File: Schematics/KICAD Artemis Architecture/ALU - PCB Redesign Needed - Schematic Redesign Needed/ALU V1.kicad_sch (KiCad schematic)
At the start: 11 parts, among them J1 B Input Socket, J2 A Input Socket, J3 F Output Socket, J4 Control Word Socket, J5 Flag Socket, J6 Power Socket, U1 74LS181, U2 74LS181, U3 74LS30

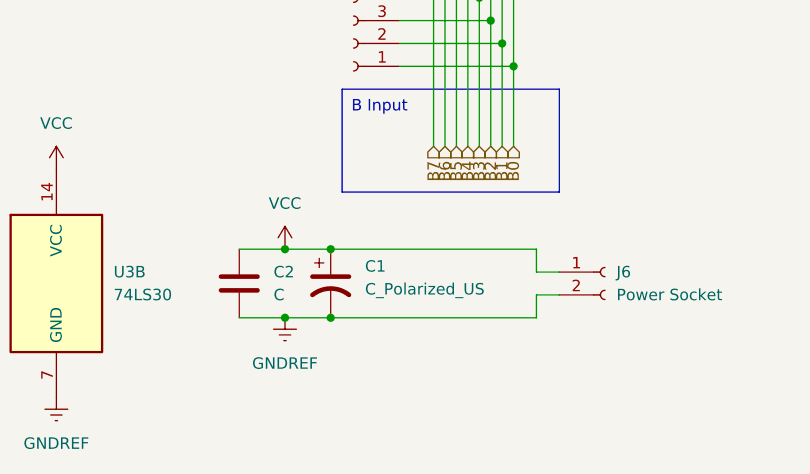
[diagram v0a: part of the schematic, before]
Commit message: Started ALU redesign
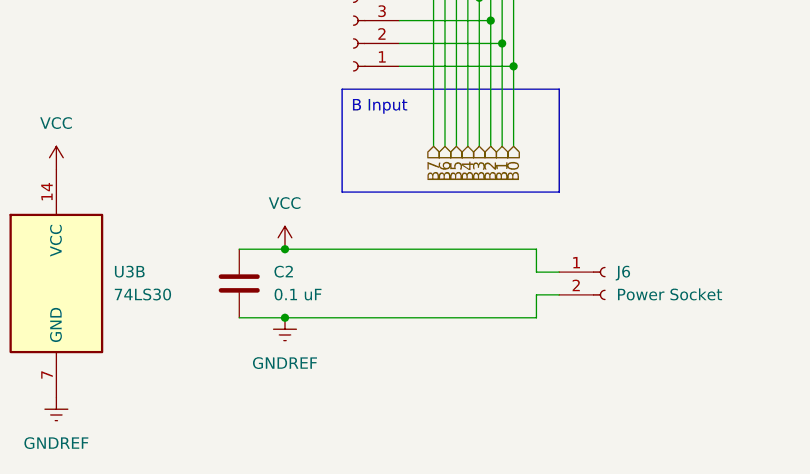
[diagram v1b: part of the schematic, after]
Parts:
- removed C1: C_Polarized_US, Capacitor_THT:CP_Radial_D10.0mm_P5.00mm, symbol Device:C_Polarized_US
- C2: value C -> 0.1 uF; footprint Capacitor_THT:C_Disc_D3.0mm_W2.0mm_P2.50mm -> Capacitor_SMD:C_1206_3216Metric_Pad1.33x1.80mm_HandSolder
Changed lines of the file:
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@@
 	)
 	(junction
-		(at 78.74 172.72)
-		(diameter 0)
-		(color 0 0 0 0)
-	)
-	(junction
 		(at 95.25 40.64)
 		(diameter 0)
@@
 	)
 	(junction
-		(at 78.74 180.34)
-		(diameter 0)
-		(color 0 0 0 0)
-	)
-	(junction
 		(at 93.98 142.24)
 		(diameter 0)
@@
 	(wire
 		(pts
-			(xy 101.6 180.34) (xy 78.74 180.34)
+			(xy 73.66 180.34) (xy 101.6 180.34)
 		)
 		(stroke
@@
 	(wire
 		(pts
-			(xy 73.66 172.72) (xy 78.74 172.72)
-		)
-		(stroke
-			(width 0)
-			(type default)
-		)
-	)
-	(wire
-		(pts
 			(xy 191.77 57.15) (xy 191.77 88.9)
 		)
@@
 	(wire
 		(pts
-			(xy 73.66 180.34) (xy 78.74 180.34)
-		)
-		(stroke
-			(width 0)
-			(type default)
-		)
-	)
-	(wire
-		(pts
 			(xy 86.36 149.86) (xy 97.79 149.86)
 		)
@@
 	(wire
 		(pts
-			(xy 101.6 172.72) (xy 78.74 172.72)
+			(xy 73.66 172.72) (xy 101.6 172.72)
 		)
 		(stroke
@@
 			)
 		)
-		(property "Value" "C"
+		(property "Value" "0.1 uF"
 			(at 72.39 177.7999 0)
 			(effects
@@
 			)
 		)
-		(property "Footprint" "Capacitor_THT:C_Disc_D3.0mm_W2.0mm_P2.50mm"
+		(property "Footprint" "Capacitor_SMD:C_1206_3216Metric_Pad1.33x1.80mm_HandSolder"
 			(at 69.5452 180.34 0)
 			(effects
@@
 					(unit 1)
 				)
-			)
-		)
-	)
-	(symbol
-		(lib_id "Device:C_Polarized_US")
-		(at 78.74 176.53 0)
-		(unit 1)
-		(exclude_from_sim no)
-		(in_bom yes)
-		(on_board yes)
-		(dnp no)
-		(fields_autoplaced yes)
-		(property "Reference" "C1"
-			(at 82.55 174.6249 0)
-			(effects
-				(font
-					(size 1.27 1.27)
-				)
-				(justify left)
-			)
-		)
-		(property "Value" "C_Polarized_US"
-			(at 82.55 177.1649 0)
-			(effects
-				(font
-					(size 1.27 1.27)
-				)
-				(justify left)
-			)
-		)
-		(property "Footprint" "Capacitor_THT:CP_Radial_D10.0mm_P5.00mm"
-			(at 78.74 176.53 0)
-			(effects
-				(font
-					(size 1.27 1.27)
-				)
-				(hide yes)
-			)
-		)
-		(property "Datasheet" "~"
-			(at 78.74 176.53 0)
-			(effects
-				(font
-					(size 1.27 1.27)
-				)
-				(hide yes)
-			)
-		)
-		(property "Description" "Polarized capacitor, US symbol"
-			(at 78.74 176.53 0)
-			(effects
-				(font
-					(size 1.27 1.27)
-				)
-				(hide yes)
-			)
-		)
-		(pin "2"
-		)
-		(pin "1"
-		)
-		(instances
-			(project ""
-				(path "/c35394b0-d1ff-42b6-ad6e-0a155b8effb2"
-					(reference "C1")
-					(unit 1)
-				)
-			)
-			(project ""
-				(path "/e5aa38bc-c1b3-42af-8692-454c67b5224c/7429cd68-8649-41c9-882b-528396eb7a0e"
-					(reference "C1")
-					(unit 1)
-				)

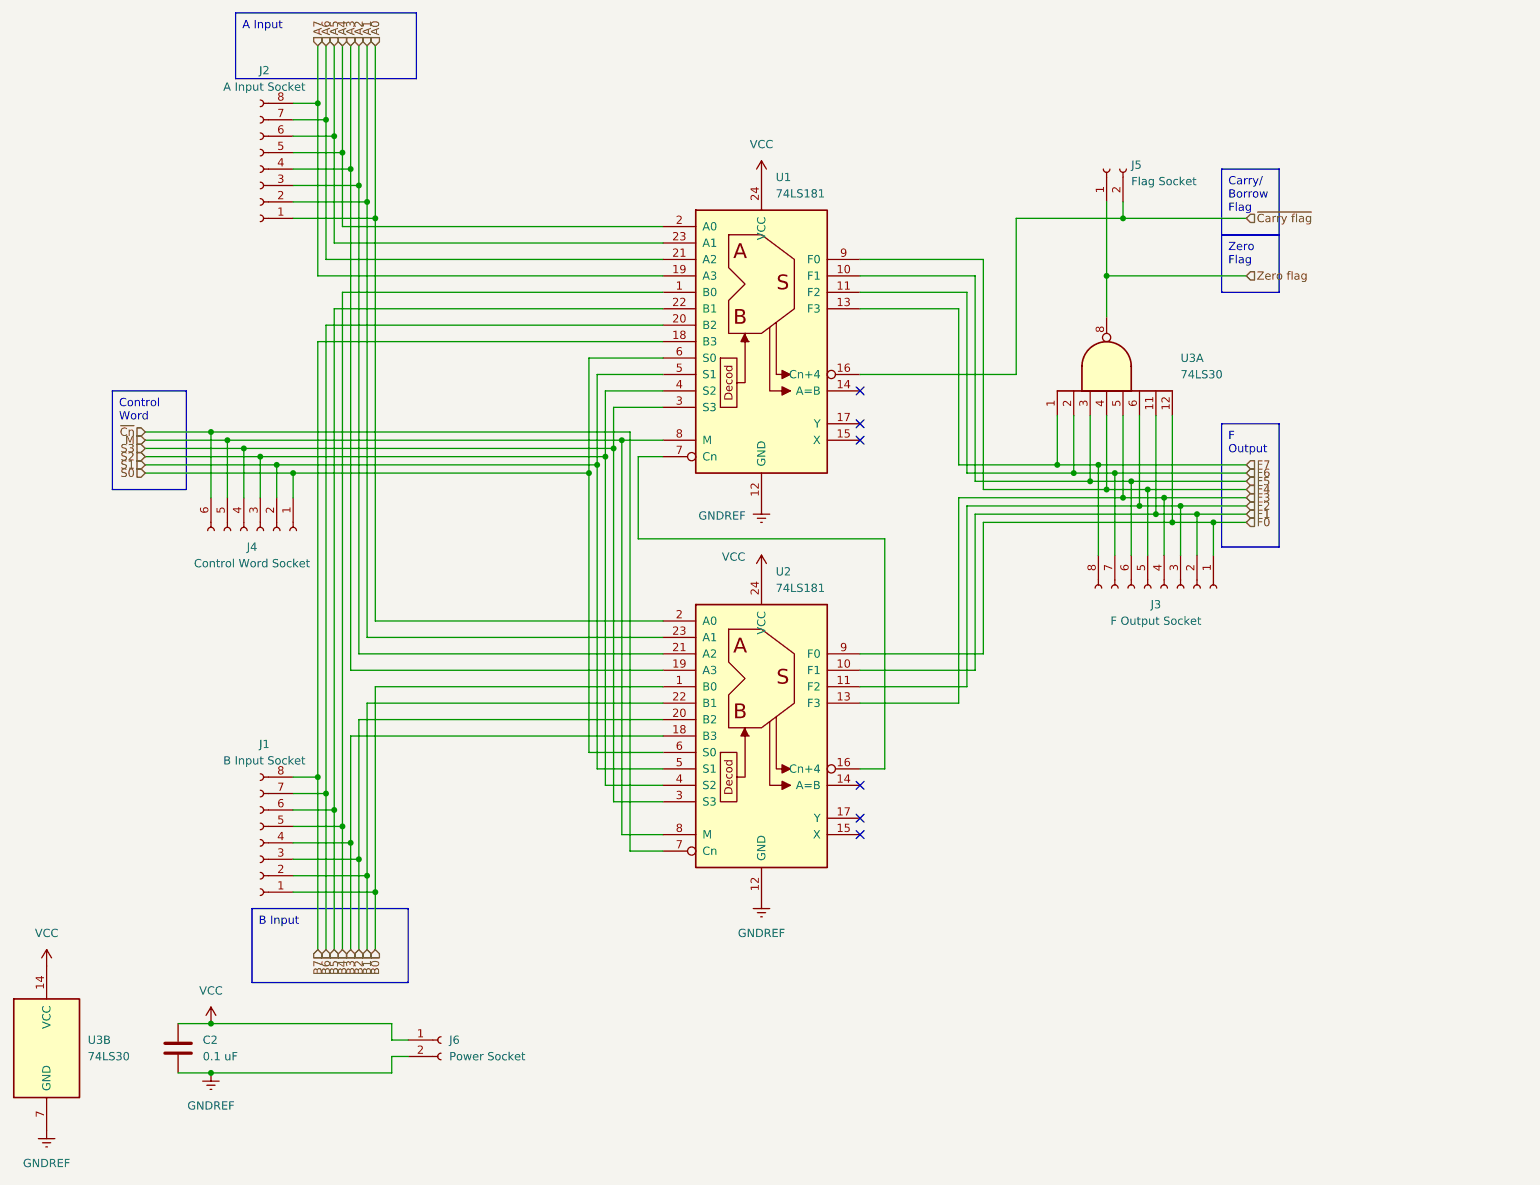
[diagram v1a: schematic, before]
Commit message: ALU Schematic Redesign
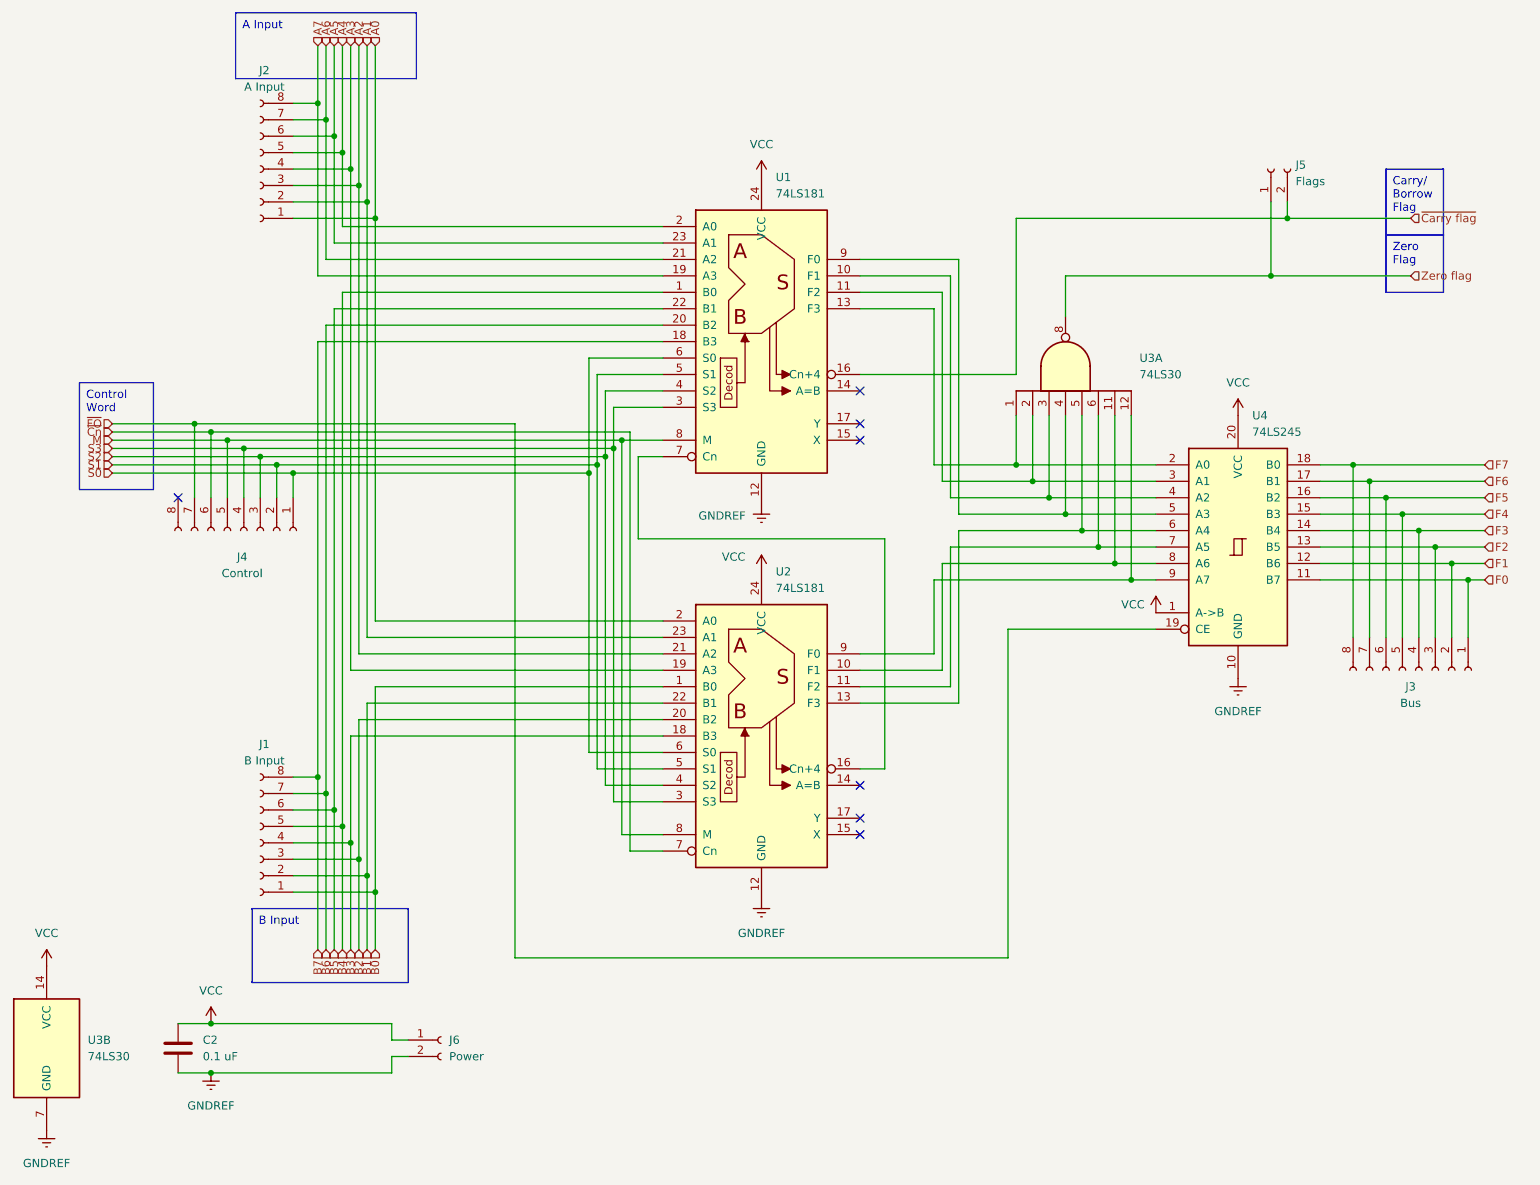
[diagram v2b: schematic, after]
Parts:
- removed J4: Control Word Socket, Connector_Molex:Molex_PicoBlade_53048-0610_1x06_P1.25mm_Horizontal, symbol Connector:Conn_01x06_Socket
- added J4: Control, Connector_Molex:Molex_PicoBlade_53048-0810_1x08_P1.25mm_Horizontal, symbol Connector:Conn_01x08_Socket
- added U4: 74LS245, Package_DIP:DIP-20_W7.62mm_Socket_LongPads, symbol 74xx:74LS245
- J1: value B Input Socket -> B Input
- J2: value A Input Socket -> A Input
- J3: value F Output Socket -> Bus
- J5: value Flag Socket -> Flags
- J6: value Power Socket -> Power
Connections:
- net F0: now also U4.11 (B7); no longer U2.9 (F0), U3.12
- net F1: now also U4.12 (B6); no longer U2.10 (F1), U3.11
- net F2: now also U4.13 (B5); no longer U2.11 (F2), U3.6
- net F3: now also U4.14 (B4); no longer U2.13 (F3), U3.5
- net F4: now also U4.15 (B3); no longer U1.9 (F0), U3.4
- net F5: now also U4.16 (B2); no longer U1.10 (F1), U3.3
- net F6: now also U4.17 (B1); no longer U1.11 (F2), U3.2
- net F7: now also U4.18 (B0); no longer U1.13 (F3), U3.1
- net GNDREF: now also U4.10 (GND)
- net M: now also J4.5 (Pin_5)
- net S0: now also J4.1 (Pin_1)
- net S1: now also J4.2 (Pin_2)
- net S2: now also J4.3 (Pin_3)
- net S3: now also J4.4 (Pin_4)
- net VCC: now also U4.1 (A->B), U4.20 (VCC)
- net ~{Cn}: now also J4.6 (Pin_6)
- new net: U1.13 (F3), U3.1, U4.2 (A0)
- new net: U1.11 (F2), U3.2, U4.3 (A1)
- new net: U1.10 (F1), U3.3, U4.4 (A2)
- new net: U1.9 (F0), U3.4, U4.5 (A3)
- new net: U2.13 (F3), U3.5, U4.6 (A4)
- new net: U2.11 (F2), U3.6, U4.7 (A5)
- new net: U2.10 (F1), U3.11, U4.8 (A6)
- new net: U2.9 (F0), U3.12, U4.9 (A7)
- new net ~{FO}: J4.7 (Pin_7), U4.19 (CE)
- no-connect marks 6 -> 7
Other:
- moved on the sheet: J3, J5, U3A
